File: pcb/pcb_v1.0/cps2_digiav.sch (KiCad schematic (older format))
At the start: 6 parts, among them U7 TC1262-3.3VDBTR, U8 TLV70033

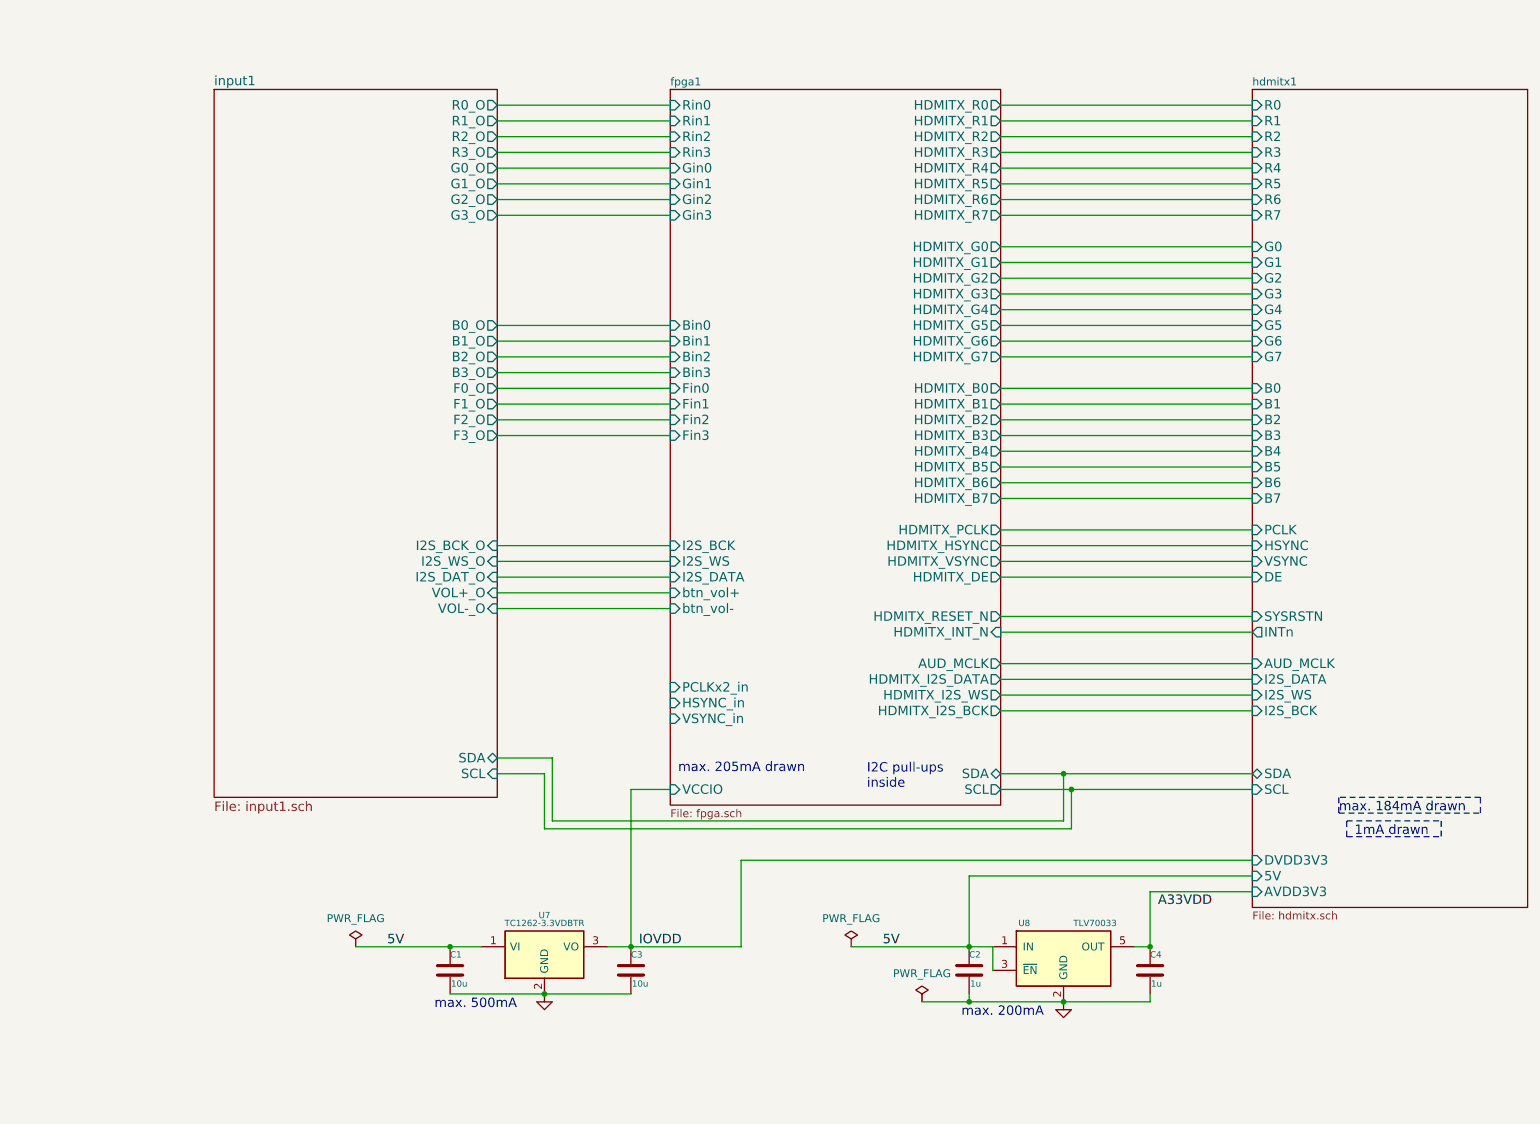
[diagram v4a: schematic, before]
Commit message: Reordered inputs, improved clock layout
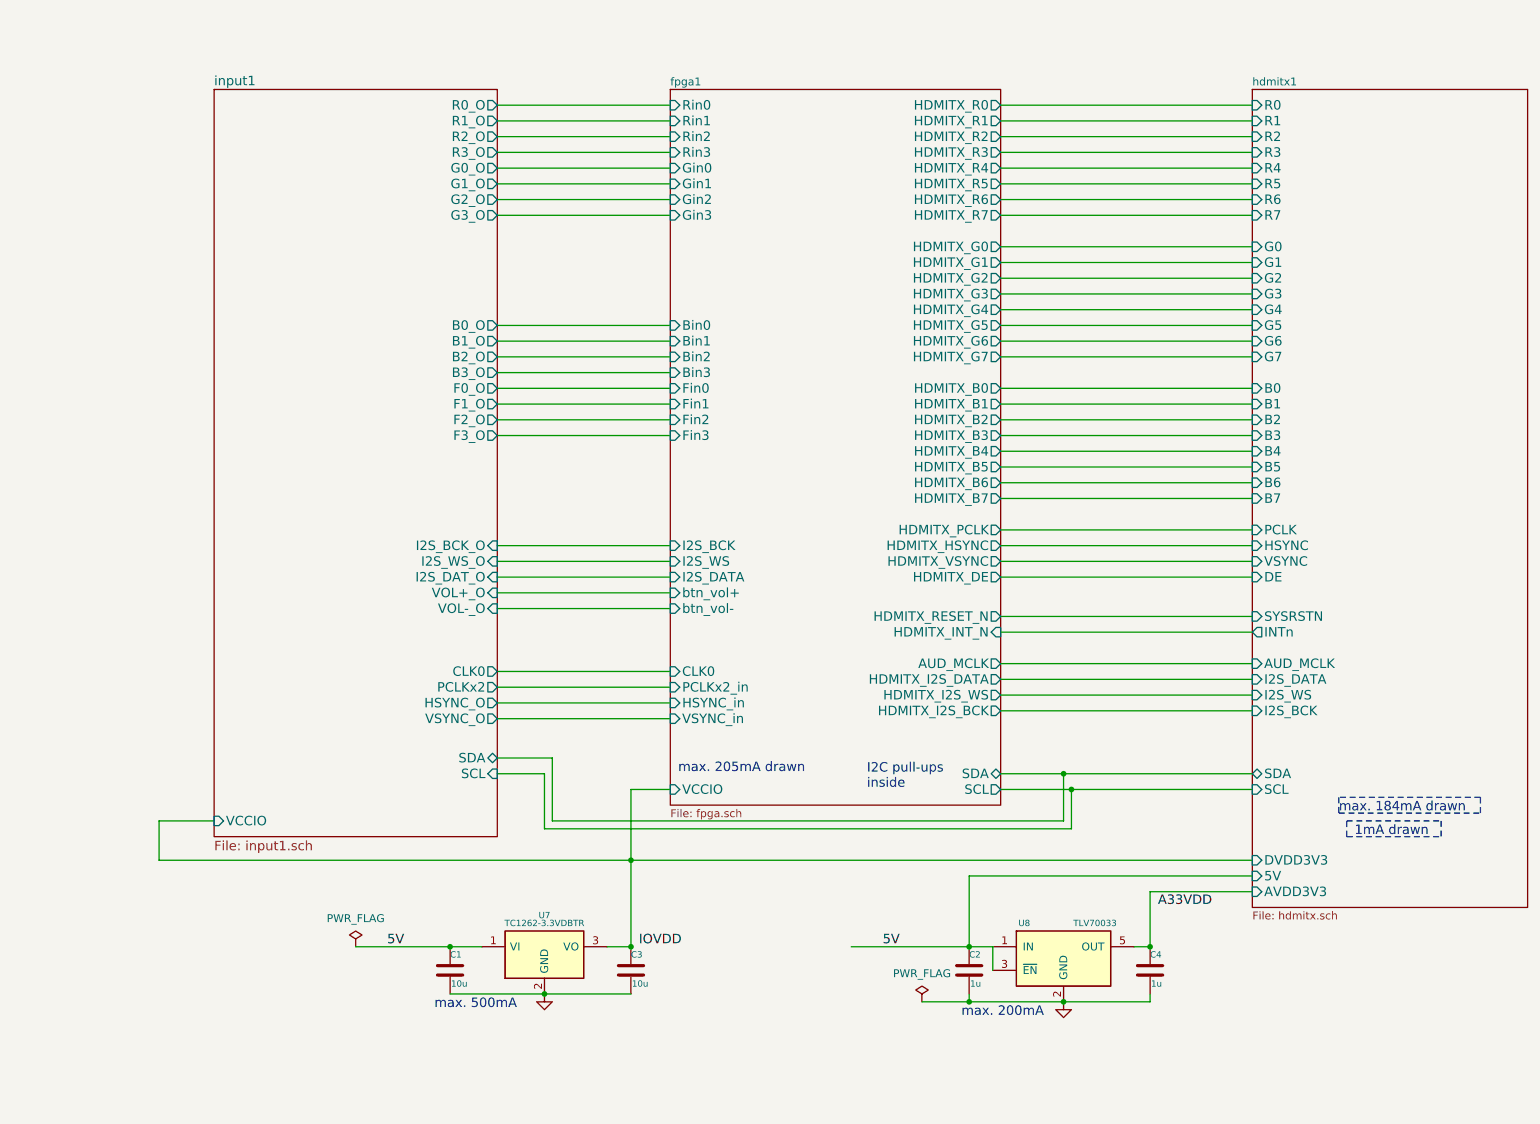
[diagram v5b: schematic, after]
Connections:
- net IOVDD: no longer C3.1, U7.3 (VO)
- new net fpga1/VCCIO: C3.1, U7.3 (VO)
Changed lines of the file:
@@
 LIBS:valves
 LIBS:custom_components
-LIBS:HDMI
 LIBS:74lvc
 LIBS:altera
@@
 LIBS:usb3_micro_ab
 LIBS:wolfson
+LIBS:ossc_board-cache
 LIBS:cps2_digiav-cache
 EELAYER 25 0
@@
 $EndComp
 $Comp
-L PWR_FLAG #FLG06
+L PWR_FLAG #FLG03
 U 1 1 57EB0658
 P 2650 6650
-F 0 "#FLG06" H 2650 6745 50  0001 C CNN
+F 0 "#FLG03" H 2650 6745 50  0001 C CNN
 F 1 "PWR_FLAG" H 2650 6830 50  0000 C CNN
 F 2 "" H 2650 6650 50  0000 C CNN
@@
 5V
 $Comp
-L PWR_FLAG #FLG021
+L PWR_FLAG #FLG04
 U 1 1 57EB1979
 P 6250 7000
-F 0 "#FLG021" H 6250 7095 50  0001 C CNN
+F 0 "#FLG04" H 6250 7095 50  0001 C CNN
 F 1 "PWR_FLAG" H 6250 7180 50  0000 C CNN
 F 2 "" H 6250 7000 50  0000 C CNN
@@
 $EndComp
 $Sheet
-S 1750 1200 1800 4500
+S 1750 1200 1800 4750
 U 5A43CDD8
 F0 "input1" 60
@@
 F23 "SDA" B R 3550 5450 60
 F24 "SCL" I R 3550 5550 60
+F25 "HSYNC_O" O R 3550 5100 60
+F26 "VSYNC_O" O R 3550 5200 60
+F27 "PCLKx2" O R 3550 5000 60
+F28 "CLK0" O R 3550 4900 60
+F29 "VCCIO" I L 1750 5850 60
 $EndSheet
-$Comp
-L PWR_FLAG #FLG?
-U 1 1 5A45EFD4
-P 5800 6650
-F 0 "#FLG?" H 5800 6745 50  0001 C CNN
-F 1 "PWR_FLAG" H 5800 6830 50  0000 C CNN
-F 2 "" H 5800 6650 50  0000 C CNN
-F 3 "" H 5800 6650 50  0000 C CNN
-	1    5800 6650
-	1    0    0    -1
-$EndComp
 Text Label 6000 6650 0    60   ~ 0
 5V
@@
 F61 "HDMITX_I2S_WS" O R 6750 5050 60
 F62 "HDMITX_I2S_BCK" O R 6750 5150 60
+F63 "CLK0" I L 4650 4900 60
 $EndSheet
 Wire Wire Line
@@
 Connection ~ 3250 6650
 Connection ~ 4400 6650
-Wire Wire Line
-	4250 6650 5100 6650
 Connection ~ 7150 7000
 Wire Wire Line
@@
 	6550 6200 8350 6200
 Wire Wire Line
-	5100 6100 8350 6100
-Wire Wire Line
-	5100 6650 5100 6100
+	1400 6100 8350 6100
 Wire Wire Line
 	4650 5650 4400 5650
@@
 Wire Wire Line
 	6750 5150 8350 5150
+Wire Wire Line
+	4400 6650 4250 6650
+Connection ~ 4400 6100
+Wire Wire Line
+	1400 6100 1400 5850
+Wire Wire Line
+	1400 5850 1750 5850
+Wire Wire Line
+	3550 5000 4650 5000
+Wire Wire Line
+	3550 5100 4650 5100
+Wire Wire Line
+	3550 5200 4650 5200
+Wire Wire Line
+	3550 4900 4650 4900
 $EndSCHEMATC
